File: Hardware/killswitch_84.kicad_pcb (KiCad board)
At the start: 2 copper layers, 25 x 56 mm, 29 parts, among them J1 PWR_IN, J2 BTN/LED, J3 PI, Q1 Q_PMOS_GSD, SW1 SW_Push, U1 ATTINY84-20SSU, U2 TSDP341xx, U3 AZ1117-3.3, U4 TXB0108DQSR

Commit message: updated pcb
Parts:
- moved ? 6.20 mm to (153.1, 77.2)
- moved R4 2.06 mm to (153.9, 108.5)
- moved C6 1.52 mm to (137.9, 82.3)
- moved C7 0.76 mm to (137.9, 85.1)
- turned C5 to 180 degrees
- turned R6 to 180 degrees
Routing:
- net +5V: track 0.00 -> 87.9 mm
- net GND: track 0.00 -> 71.5 mm, vias 0 -> 9
- net LED: track 0.00 -> 42.3 mm, vias 0 -> 1
- net +3V3: track 0.00 -> 41.6 mm, vias 0 -> 2
- net TX_P: track 0.00 -> 39.0 mm, vias 0 -> 1
- net BTN: track 0.00 -> 38.0 mm
- net RX_P: track 0.00 -> 32.1 mm, vias 0 -> 1
- net MISO_P: track 0.00 -> 29.6 mm
- net Net-(U1-Pad12): track 0.00 -> 28.9 mm, vias 0 -> 1
- net SCK_P: track 0.00 -> 27.8 mm
- net MOSI_P: track 0.00 -> 26.9 mm
- net TR_P: track 0.00 -> 25.3 mm, vias 0 -> 1
- net RST_P: track 0.00 -> 24.5 mm, vias 0 -> 1
- net FB_P: track 0.00 -> 22.5 mm, vias 0 -> 1
- net RST_A: track 0.00 -> 20.0 mm, vias 0 -> 2
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- added copper zone on B.Cu, net GND
- added copper zone on F.Cu, net GND
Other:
- net class Default: clearance 0.254 -> 0.15; trace_width 0.254 -> 0.15
- net class Power: clearance 0.508 -> 0.15; trace_width 0.508 -> 0.15
- rule trace_clearance: 0.254 -> 0.15
- board text added: "KillSwitch v 0.3 b 19.02.20"

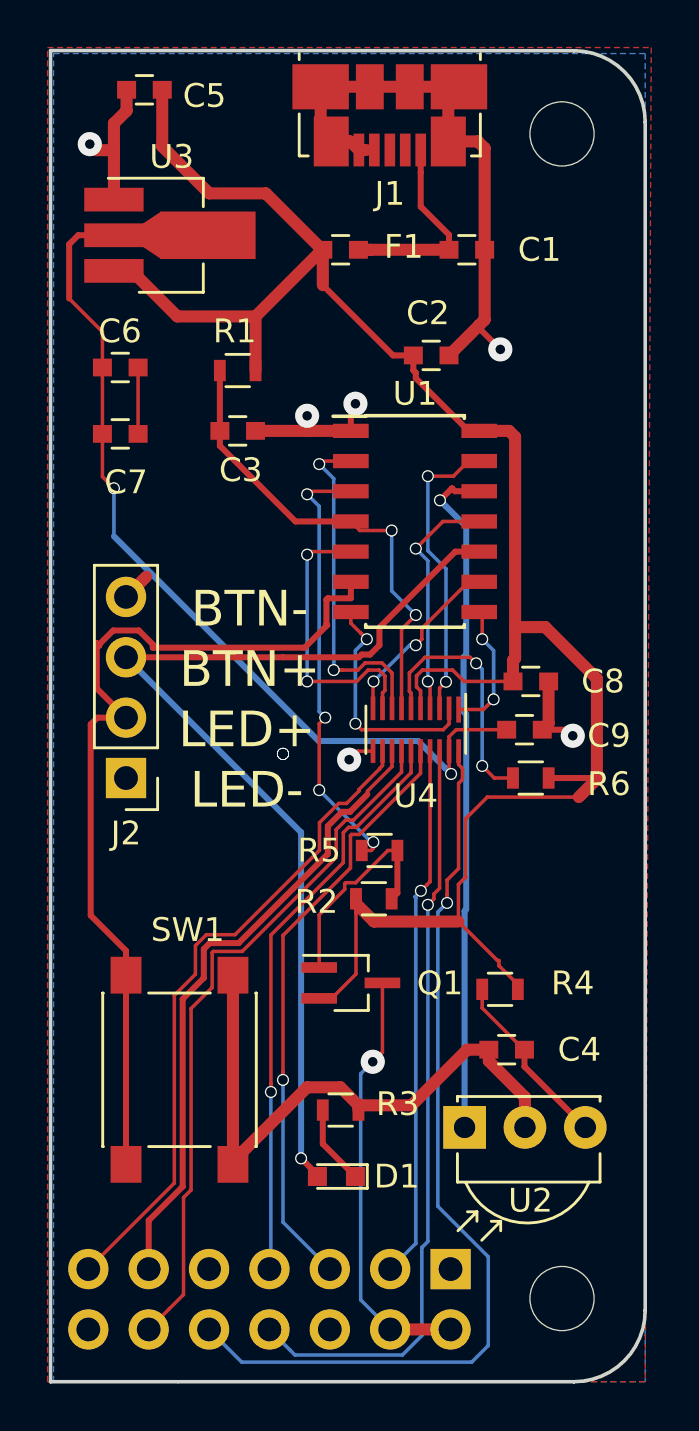
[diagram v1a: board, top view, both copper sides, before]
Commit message: added 3d view of ir receiver and hang tabs for usb connector
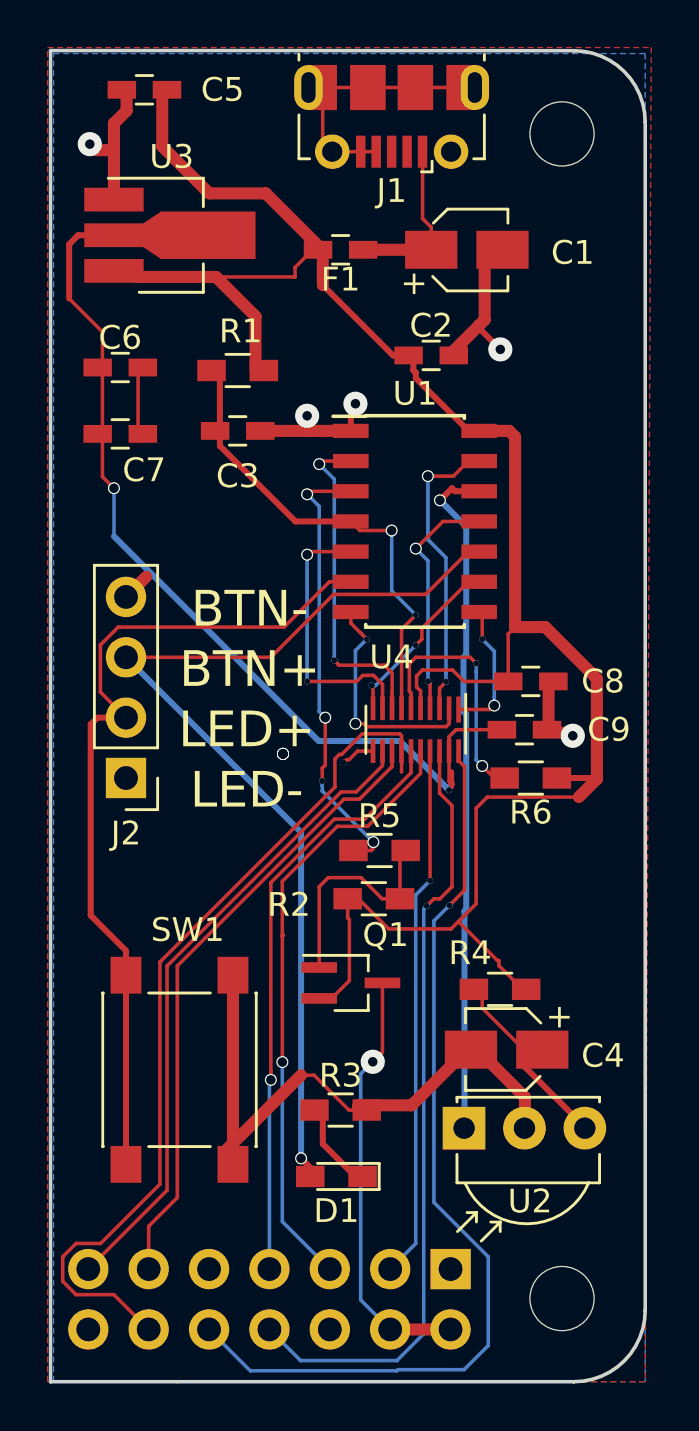
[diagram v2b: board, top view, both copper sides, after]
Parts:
- C1, C4: footprint Capacitors_SMD:C_0603 -> Capacitors_SMD:CP_Elec_3x5.3
- C2, C3, C5, C6, C7, C8, C9, F1: footprint Capacitors_SMD:C_0603 -> Capacitors_SMD:C_0603_HandSoldering
- D1: footprint LEDs:LED_0603 -> LEDs:LED_0603_HandSoldering
- J1: footprint Connectors_USB:USB_Micro-B_Molex_47346-0001 -> Connectors_USB:USB_Micro-B_Molex-105017-0001
- R1, R2, R3, R4, R5, R6: footprint Resistors_SMD:R_0603 -> Resistors_SMD:R_0603_HandSoldering
- moved J1 0.39 mm to (149.3, 70.9)
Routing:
- net GND: track 71.5 -> 64.2 mm, vias 9 -> 11
- net MISO_P: track 29.6 -> 36.6 mm
- net BTN: track 38.0 -> 35.9 mm
- net +3V3: track 41.6 -> 43.0 mm
- net +5V: track 87.9 -> 89.3 mm
- net Net-(Q1-Pad1): track 8.90 -> 9.80 mm
- net RX_P: track 32.1 -> 32.9 mm
- net TR_P: track 25.3 -> 26.0 mm
- net RST_P: track 24.5 -> 25.0 mm
- net MOSI_A: track 12.2 -> 11.7 mm
- net SCK_P: track 27.8 -> 27.3 mm
- net MOSI_P: track 26.9 -> 26.4 mm
- net TX_P: track 39.0 -> 39.5 mm
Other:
- net class Default: clearance 0.15 -> 0.1524; trace_width 0.15 -> 0.1524; via_dia 0.508 -> 0.255; via_drill 0.4 -> 0.254
- net class Power: clearance 0.15 -> 0.1524; trace_width 0.15 -> 0.1524; via_dia 1.016 -> 0.255; via_drill 0.4 -> 0.254
- rule trace_clearance: 0.15 -> 0.1524
- rule trace_min: 0.1 -> 0
- rule via_min_drill: 0.3 -> 0
- rule via_min_size: 0.4 -> 0

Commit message: added pins to header for ir
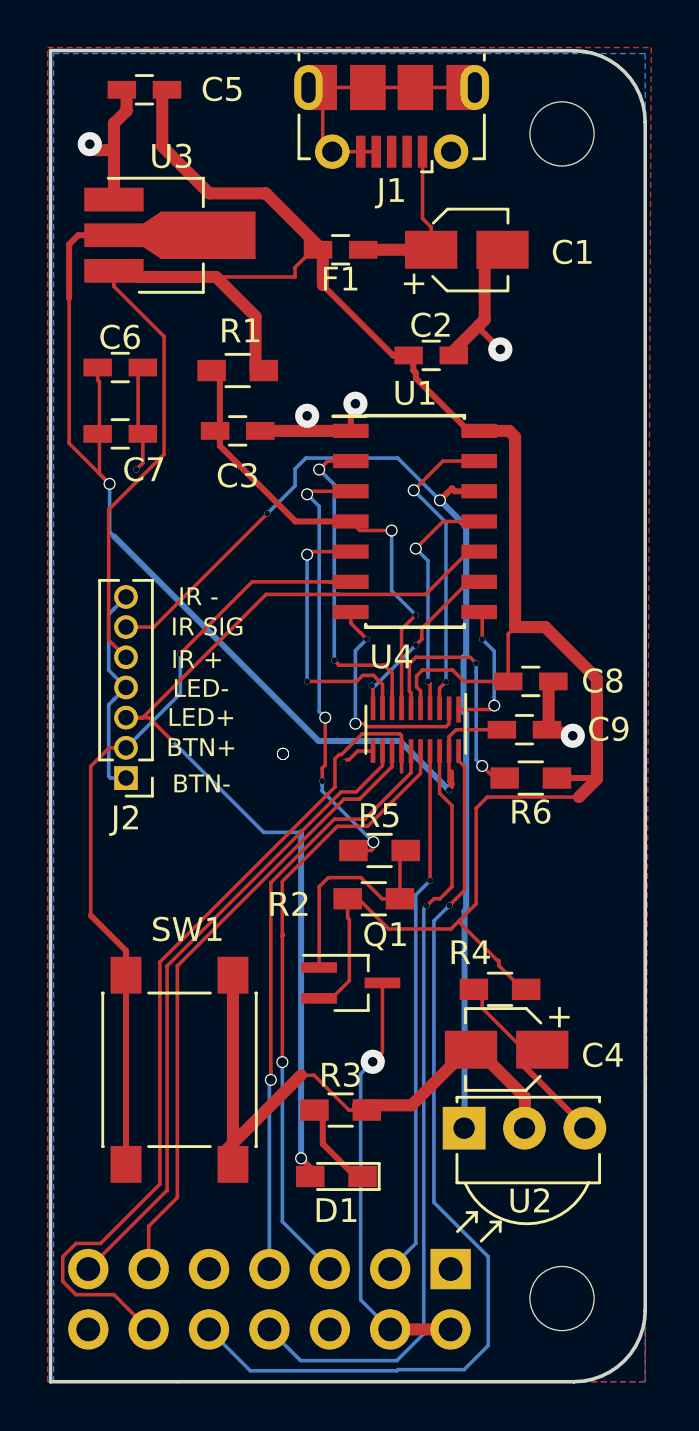
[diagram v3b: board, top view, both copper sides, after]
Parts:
- J2: value BTN/LED -> REMOTE; footprint Pin_Headers:Pin_Header_Straight_1x04_Pitch2.54mm -> Pin_Headers:Pin_Header_Straight_1x07_Pitch1.27mm
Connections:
- U1 pad 12: Net-(U1-Pad12) -> IR
- U2 pad 1: Net-(U1-Pad12) -> IR
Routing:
- net IR: track 0.00 -> 46.2 mm, vias 0 -> 2
- net Net-(U1-Pad12): track 28.9 -> 0.00 mm, vias 1 -> 0
- net +5V: track 89.3 -> 107.7 mm
- net GND: track 64.2 -> 73.8 mm, vias 11 -> 12
- net +3V3: track 43.0 -> 48.0 mm
- net BTN: track 35.9 -> 33.4 mm, vias 0 -> 1
- net LED: track 41.9 -> 42.1 mm, vias 1 -> 2
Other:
- board text added: "IR +"
- board text added: "IR -"
- board text added: "IR SIG"

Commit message: final rev 3 board
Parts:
- added D2: LED, LEDs:LED_0603_HandSoldering, F.Cu at (157.6, 76.7)
- added JP1: Jumper_NO_Small, Jumper:SolderJumper-2_P1.3mm_Bridged2Bar_Pad1.0x1.5mm, F.Cu at (157.6, 83.6)
- added R7: 1K, Resistors_SMD:R_0603_HandSoldering, F.Cu at (157.6, 80.0)
- J2: footprint Pin_Headers:Pin_Header_Straight_1x07_Pitch1.27mm -> Pin_Headers:Pin_Header_Straight_1x07_Pitch2.54mm
- moved J2 4.06 mm to (138.2, 103.7)
- moved C9 0.32 mm to (155.2, 97.6)
- moved R6 0.30 mm to (155.3, 99.3)
- moved C8 0.26 mm to (155.2, 95.3)
- moved C3 0.13 mm to (142.9, 85.1)
- moved R1 0.13 mm to (142.9, 82.3)
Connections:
- J2 pad 1: GND -> BTN
- J2 pad 2: BTN -> GND
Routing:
- net +5V: track 107.7 -> 118.4 mm, vias 0 -> 2
- net GND: track 73.8 -> 66.2 mm, vias 12 -> 6
- net Net-(JP1-Pad1): track 0.00 -> 3.77 mm
- net Net-(D2-Pad1): track 0.00 -> 3.30 mm
- net +3V3: track 48.0 -> 45.2 mm
- net BTN: track 33.4 -> 34.6 mm, vias 1 -> 0
- net IR: track 46.2 -> 45.2 mm, vias 2 -> 1
- net MISO_P: track 36.6 -> 35.7 mm
- net LED: track 42.1 -> 42.0 mm, vias 2 -> 1
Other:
- board text added: "PWR"

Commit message: moved version/build info down
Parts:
- moved ? 1.02 mm to (153.1, 78.3)
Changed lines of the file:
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@@
   )
   (module DH_Logo:DH_Logo (layer B.Cu)
-    (at 153.142 77.248 180)
+    (at 153.142 78.264 180)
     (fp_text reference "" (at -0.254 -4.826 180) (layer B.SilkS) hide
       (effects (font (size 1.524 1.524) (thickness 0.3)) (justify mirror))
@@
     (arrow2b (pts (xy 166.605124 68.993) (xy 167.191545 70.119504)))
   )
-  (gr_text "KillSwitch\nv 0.3\nb 19.02.20" (at 143.49 77.756) (layer B.SilkS)
+  (gr_text "KillSwitch\nv 0.3\nb 19.02.20" (at 143.49 78.518) (layer B.SilkS)
     (effects (font (size 1.5 1.5) (thickness 0.3)) (justify mirror))
   )

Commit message: changed version system
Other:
- board text added: "KillSwitch v 0.3.0"
- board text removed: "KillSwitch v 0.3 b 19.02.20"
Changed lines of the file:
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@@
     (title "KillSwitch on ATTiny84")
     (date 2019-02-20)
-    (rev 0.3)
+    (rev 0.3.0)
     (company "Dana Hynes")
     (comment 1 "Copyright (c) 2019 ")
@@
   )
   (layers
-    (0 F.Cu signal)
-    (31 B.Cu signal)
+    (0 F.Cu signal hide)
+    (31 B.Cu signal hide)
     (32 B.Adhes user)
     (33 F.Adhes user)
@@
     (aux_axis_origin 0 0)
     (grid_origin 160 125)
-    (visible_elements FFFDFFFF)
+    (visible_elements FFFD79FF)
     (pcbplotparams
       (layerselection 0x00030_80000001)
@@
     (arrow2b (pts (xy 166.605124 68.993) (xy 167.191545 70.119504)))
   )
-  (gr_text "KillSwitch\nv 0.3\nb 19.02.20" (at 143.49 78.518) (layer B.SilkS)
+  (gr_text "KillSwitch\nv 0.3.0" (at 143.49 78.518) (layer B.SilkS)
     (effects (font (size 1.5 1.5) (thickness 0.3)) (justify mirror))
   )

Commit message: rc for changing the update code (again)
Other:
- board text added: "KillSwitch v 0.3.2"
- board text removed: "KillSwitch v 0.3.0"
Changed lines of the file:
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@@
   (title_block
     (title "KillSwitch on ATTiny84")
-    (date 2019-02-20)
-    (rev 0.3.0)
+    (date 2019-02-25)
+    (rev 0.3.2)
     (company "Dana Hynes")
     (comment 1 "Copyright (c) 2019 ")
@@
     (arrow2b (pts (xy 166.605124 68.993) (xy 167.191545 70.119504)))
   )
-  (gr_text "KillSwitch\nv 0.3.0" (at 143.49 78.518) (layer B.SilkS)
+  (gr_text "KillSwitch\nv 0.3.2" (at 143.49 78.518) (layer B.SilkS)
     (effects (font (size 1.5 1.5) (thickness 0.3)) (justify mirror))
   )

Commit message: new version number
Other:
- board text added: "KillSwitch v 0.3.3"
- board text removed: "KillSwitch v 0.3.2"
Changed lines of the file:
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@@
     (title "KillSwitch on ATTiny84")
     (date 2019-02-25)
-    (rev 0.3.2)
+    (rev 0.3.3)
     (company "Dana Hynes")
     (comment 1 "Copyright (c) 2019 ")
@@
     (aux_axis_origin 0 0)
     (grid_origin 160 125)
-    (visible_elements FFFD79FF)
+    (visible_elements FFFC7FFF)
     (pcbplotparams
       (layerselection 0x00030_80000001)
@@
     (arrow2b (pts (xy 166.605124 68.993) (xy 167.191545 70.119504)))
   )
-  (gr_text "KillSwitch\nv 0.3.2" (at 143.49 78.518) (layer B.SilkS)
+  (gr_text "KillSwitch\nv 0.3.3" (at 143.49 78.518) (layer B.SilkS)
     (effects (font (size 1.5 1.5) (thickness 0.3)) (justify mirror))
   )
